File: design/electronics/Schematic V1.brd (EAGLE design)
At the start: 152.4 x 149.3 mm, 170 parts, among them J1 PJ-202AH, J2 PJ-025, J3 DD50P564GTXLF, J4 DD50P564GTXLF, J5 SAMTEC-TST-105-01-X-DJ, J6 SSW-106-02-TM-S-RA, SW1 TL6330AF200Q, U1 STM32F207VGT6TR, U10 SN65LBC175ADD16-M, U11 MAX7375AXR805+T21-0075D_MXM-M, U12 SN75ALS174ADWRDW20-M, U13 SN75468DRD0016A_M, U14 SN75468DRD0016A_M, U15 ACSL-6400-00TESOIC_6400-00TE-M, U16 ACSL-6400-00TESOIC_6400-00TE-M, U17 SN65LBC175ADD16-M, U18 SN65LBC175ADD16-M, U19 SN65LBC175ADD16-M, U2 LM2678S-5.0/NOPBTS7B-M, U21 RS0104YQTSSOP-14_JRT-M, U22 RS0104YQTSSOP-14_JRT-M, U24 RS0104YQTSSOP-14_JRT-M, U3 CDBC520-GCDBC-G-M, U4 TLV1117LV33DCYR, U5 LM43601PWPRPWP16_TEX-M, U6 RS0104YQTSSOP-14_JRT-M, U7 SN75ALS174ADWRDW20-M, U8 OPA4205APWRTSSOP14_PW_R-PDSO-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

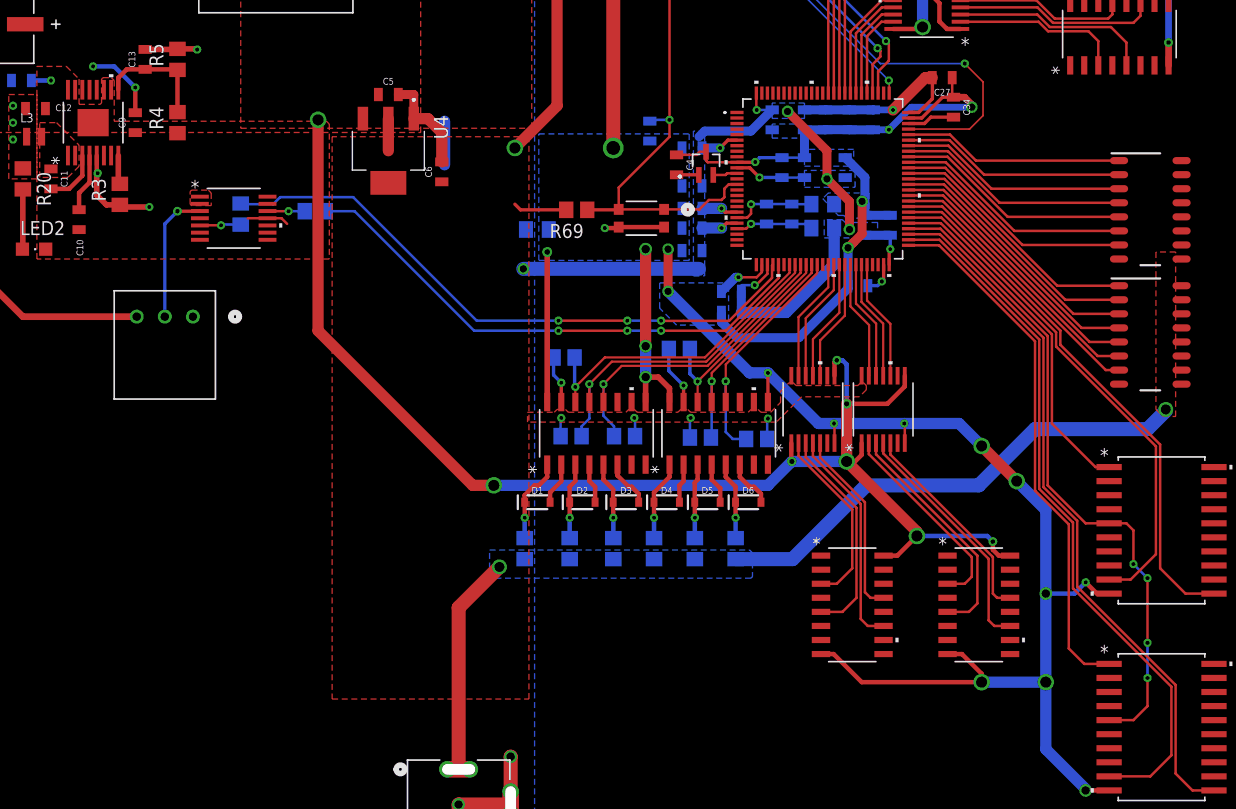
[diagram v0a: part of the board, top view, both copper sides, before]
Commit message: Updated Layout with most traces
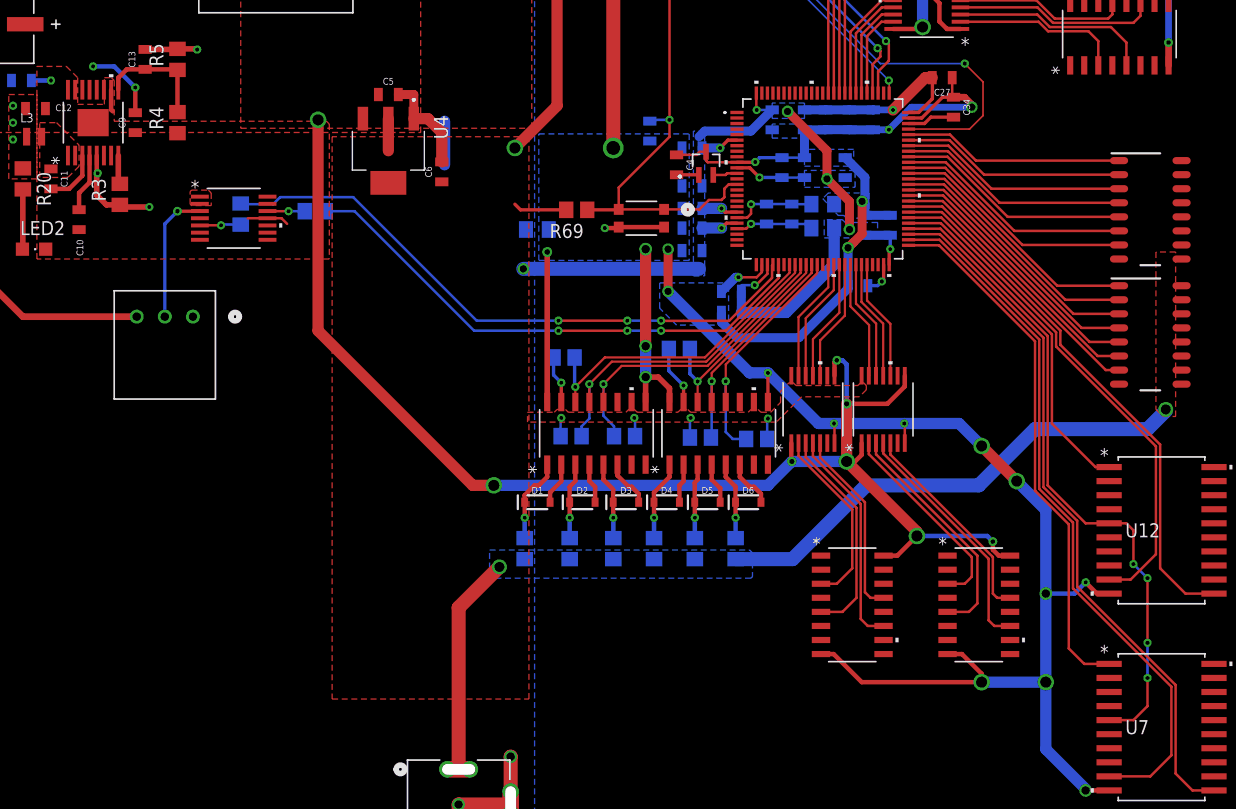
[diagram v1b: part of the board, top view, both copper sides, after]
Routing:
- net -15V: track 5.53 -> 7.55 mm
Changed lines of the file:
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@@
 <attribute name="MANUFACTURER_PART_NUMBER" value="SN75ALS174ADWR" x="306.07" y="-70.104" size="1.778" layer="27" display="off"/>
 <attribute name="MFR_NAME" value="Texas Instruments" x="306.07" y="-70.104" size="1.778" layer="27" display="off"/>
+<attribute name="NAME" x="112.2934" y="34.671" size="1.27" layer="27" ratio="6" rot="SR0"/>
 <attribute name="NAME" x="112.2934" y="34.671" size="1.27" layer="25" ratio="6" rot="SR0"/>
-<attribute name="NAME" x="112.2934" y="34.671" size="1.27" layer="27" ratio="6" rot="SR0"/>
 <attribute name="VALUE" x="113.8428" y="34.671" size="1.27" layer="27" ratio="6" rot="SR0"/>
 </element>
@@
 <attribute name="MANUFACTURER_PART_NUMBER" value="SN75ALS174ADWR" x="266.7" y="-87.884" size="1.778" layer="27" display="off"/>
 <attribute name="MFR_NAME" value="Texas Instruments" x="266.7" y="-87.884" size="1.778" layer="27" display="off"/>
+<attribute name="NAME" x="112.2934" y="16.891" size="1.27" layer="27" ratio="6" rot="SR0"/>
 <attribute name="NAME" x="112.2934" y="16.891" size="1.27" layer="25" ratio="6" rot="SR0"/>
-<attribute name="NAME" x="112.2934" y="16.891" size="1.27" layer="27" ratio="6" rot="SR0"/>
 <attribute name="VALUE" x="113.8428" y="16.891" size="1.27" layer="27" ratio="6" rot="SR0"/>
 </element>
@@
 <contactref element="C1" pad="2"/>
 <contactref element="C2" pad="1"/>
-<polygon width="0.1524" layer="1" isolate="0.508" thermals="no" rank="4">
+<polygon width="0.1524" layer="1" isolate="0.4064" thermals="no" rank="4">
 <vertex x="0" y="120.396"/>
 <vertex x="0" y="71.374"/>
@@
 <wire x1="11.176" y1="104.8258" x2="-15.56" y2="284.48" width="0" layer="19" extent="1-1"/>
 <wire x1="18.075" y1="75.1078" x2="18.725003125" y2="75.1078" width="0" layer="19" extent="1-1"/>
-<wire x1="19.375" y1="75.1078" x2="18.725003125" y2="75.1078" width="0" layer="19" extent="1-1"/>
 <wire x1="28.69565" y1="63.5" x2="22.86" y2="73.036" width="0" layer="19" extent="1-1"/>
 </signal>
@@
 <vertex x="13.97" y="77.216"/>
 <vertex x="16.637" y="77.216"/>
-<vertex x="17.78" y="76.073"/>
-<vertex x="17.78" y="73.787"/>
-<vertex x="19.685" y="73.787"/>
-<vertex x="19.812" y="73.914"/>
-<vertex x="19.812" y="76.073"/>
-<vertex x="19.939" y="76.2"/>
+<vertex x="17.653" y="76.2"/>
+<vertex x="17.653" y="73.787"/>
+<vertex x="20.066" y="73.787"/>
+<vertex x="20.066" y="76.2"/>
 <vertex x="20.701" y="76.2"/>
 <vertex x="20.955" y="75.946"/>
@@
 <wire x1="34.80435" y1="63.5" x2="36.068" y2="63.5" width="0.2286" layer="1"/>
 <wire x1="36.068" y1="63.5" x2="36.576" y2="62.992" width="0.2286" layer="1"/>
+<wire x1="20.675" y1="75.1078" x2="20.675" y2="73.305" width="0.4064" layer="1"/>
+<wire x1="20.675" y1="73.305" x2="20.828" y2="73.152" width="0.4064" layer="1"/>
 <wire x1="13.473" y1="75.946" x2="-124.46" y2="289.56" width="0" layer="19" extent="1-16"/>
-<wire x1="20.675" y1="75.1078" x2="17.425003125" y2="75.1078" width="0" layer="19" extent="1-1"/>
 </signal>
 <signal name="+24V">

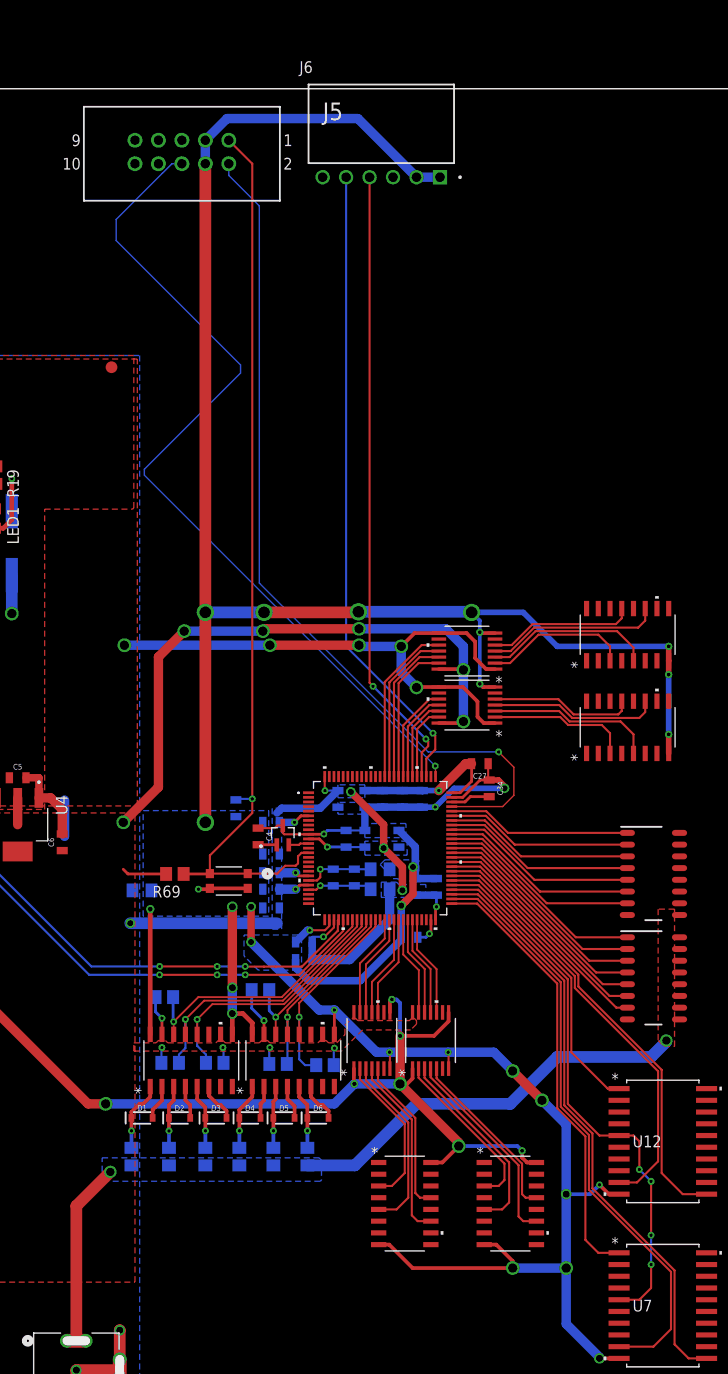
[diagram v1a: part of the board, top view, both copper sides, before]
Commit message: Moved UART signals to different pins for routing.
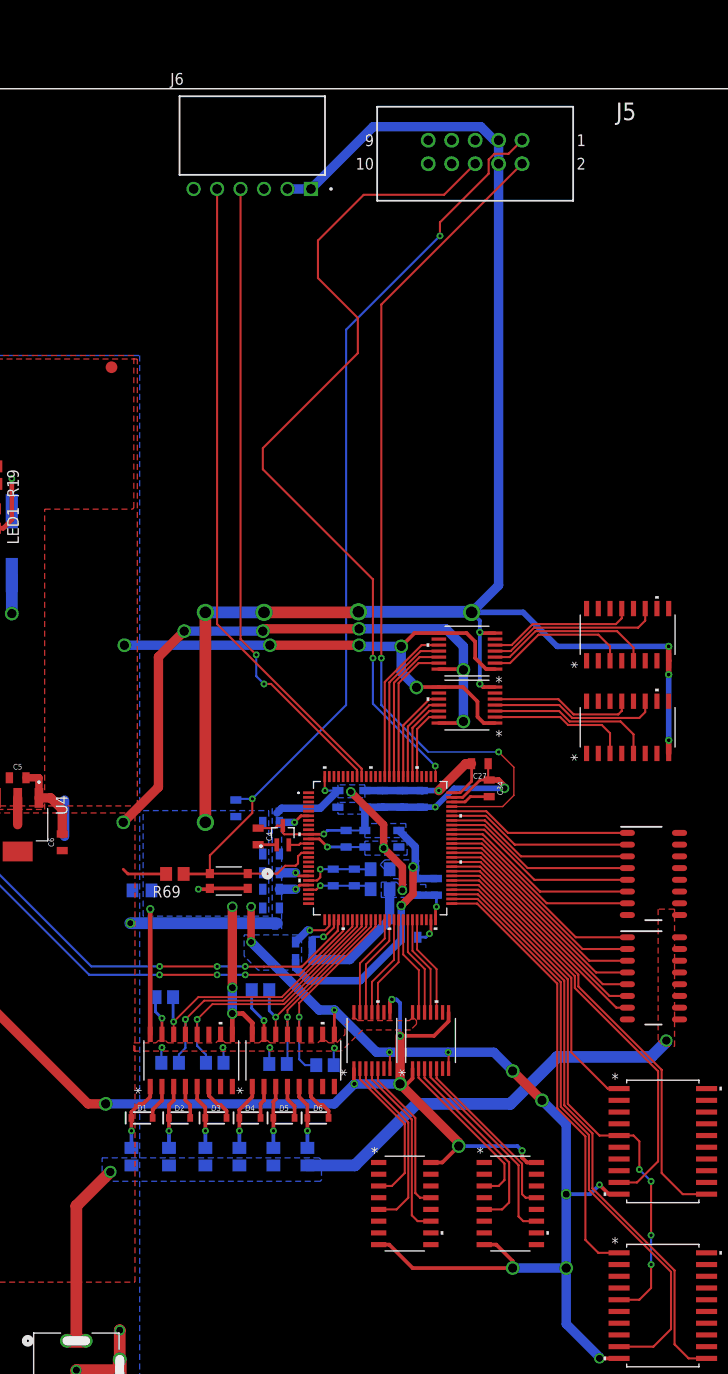
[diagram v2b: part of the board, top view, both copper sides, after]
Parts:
- moved J5 31.8 mm to (95.2, 142.2)
- moved J6 14.0 mm to (77.5, 138.4)
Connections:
- net UART_RX: now also U1.93; no longer U1.79
- net UART_TX: now also U1.92; no longer U1.78
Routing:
- net NRST: track 99.1 -> 111.0 mm, vias 1 -> 2
- net S_GND: track 404.7 -> 403.0 mm
- net UART_RX: track 67.8 -> 69.3 mm
- net UART_TX: track 69.3 -> 70.1 mm, vias 1 -> 0
- net SWCLK: track 92.9 -> 92.3 mm, vias 1 -> 2
- net SWDIO: track 92.9 -> 92.3 mm, vias 1 -> 2

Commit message: Updated schematic, added amazon order purchase
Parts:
- moved R34 344.2 mm to (94.7, 29.7), flipped to the bottom, turned to 45 degrees
- moved R33 340.6 mm to (103.9, 37.5), turned to 45 degrees
- moved R32 330.7 mm to (90.0, 32.0), flipped to the bottom, turned to 45 degrees
- moved R31 321.8 mm to (89.7, 38.0), flipped to the bottom, turned to 45 degrees
- moved C46 278.0 mm to (120.7, 47.0)
- moved C47 273.7 mm to (100.4, 43.3)
- moved J5 104.2 mm to (198.1, 125.7)
- moved J6 104.2 mm to (180.3, 121.9)
- moved U12 101.0 mm to (213.4, 9.91)
- moved U17 101.0 mm to (209.6, 64.8)
- moved U14 101.0 mm to (212.3, 38.9)
- moved R63 94.8 mm to (145.7, -8.00)
- moved U16 93.8 mm to (148.0, -15.6)
- moved D6 93.8 mm to (150.6, -21.8)
- moved R30 93.8 mm to (149.5, -26.0)
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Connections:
- net ABS_ENC_OUT_GPIO_1: now also U1.44; no longer U1.83
- net ABS_ENC_OUT_GPIO_2: no longer U1.87
- net ALARM_RST_AN_1: now also U13.14; no longer U13.12
- net ALARM_RST_GPIO_1: now also U1.38, U13.3; no longer U1.60, U13.5
- net ALARM_RST_GPIO_2: no longer U1.67
- net ALO_GPIO_A_1: now also U1.31; no longer U1.32
- net ALO_GPIO_A_2: no longer U1.35
- net ALO_GPIO_B_1: now also U1.32; no longer U1.33
- net ALO_GPIO_B_2: no longer U1.36
- net ALO_GPIO_C_1: now also U1.33; no longer U1.34
- net ALO_GPIO_C_2: no longer U1.37
- net CLR_GPIO_2: no longer U1.57
- net DIR_GPIO_2: no longer U1.56
- net ENC_PUL_OUT_A_GPIO_1: now also U1.41; no longer U1.80
- net ENC_PUL_OUT_A_GPIO_2: no longer U1.84
- net ENC_PUL_OUT_B_GPIO_1: now also U1.42; no longer U1.81
- net ENC_PUL_OUT_B_GPIO_2: no longer U1.85
- net ENC_PUL_OUT_C_GPIO_1: now also U1.43; no longer U1.82
- net ENC_PUL_OUT_C_GPIO_2: no longer U1.86
- net FRWD_DRIVE_EN_AN_1: now also U13.12; no longer U13.14
- net FRWD_DRIVE_EN_GPIO_1: now also U1.36, U13.5; no longer U1.62, U13.3
- net FRWD_DRIVE_EN_GPIO_2: no longer U1.69
- net FRWD_EX_TORQUE_LIM_EN_AN_1: now also U13.15; no longer U13.11
- net FRWD_EX_TORQUE_LIM_EN_GPIO_1: now also U1.39, U13.2; no longer U1.59, U13.6
- net FRWD_EX_TORQUE_LIM_EN_GPIO_2: no longer U1.66
- net GEN_PURPOSE_OUT_GPIO_A_1: now also U1.45; no longer U1.39
- net GEN_PURPOSE_OUT_GPIO_A_2: no longer U1.43
- net GEN_PURPOSE_OUT_GPIO_B_1: now also U1.46; no longer U1.40
- net GEN_PURPOSE_OUT_GPIO_B_2: no longer U1.44
- net GEN_PURPOSE_OUT_GPIO_C_1: now also U1.47; no longer U1.41
- net GEN_PURPOSE_OUT_GPIO_C_2: no longer U1.45
- net PROP_CONTROL_EN_AN_1: now also U13.11; no longer U13.15
- net PROP_CONTROL_EN_GPIO_1: now also U1.35, U13.6; no longer U1.63, U13.2
- net PROP_CONTROL_EN_GPIO_2: no longer U1.70
- net PULSE_GPIO_2: no longer U1.55
- net REVERSE_DRIVE_EN_GPIO_1: now also U1.37; no longer U1.61
- net REVERSE_DRIVE_EN_GPIO_2: no longer U1.68
- net REVERSE_EX_TORQUE_LIM_EN_AN_1: now also U13.16; no longer U13.10
- net REVERSE_EX_TORQUE_LIM_EN_GPIO_1: now also U1.40, U13.1; no longer U1.58, U13.7
- net REVERSE_EX_TORQUE_LIM_EN_GPIO_2: no longer U1.65
- net SERVO_ALARM_OUT_GPIO_1: now also U1.48; no longer U1.42
- net SERVO_ALARM_OUT_GPIO_2: no longer U1.46
- net SERVO_EN_AN_1: now also U13.10; no longer U13.16
- net SERVO_EN_GPIO_1: now also U1.34, U13.7; no longer U1.64, U13.1
- net SERVO_EN_GPIO_2: no longer U1.71
- net UART_RX: no longer U1.93
- net UART_TX: no longer U1.92
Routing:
- net S_GND: track 403.0 -> 161.6 mm, vias 33 -> 20
- net ENC_PUL_OUT_A_HI_1: track 0.00 -> 102.7 mm, vias 0 -> 4
- net TORQUE-SPEED_ANALOG_1: track 0.00 -> 102.4 mm, vias 0 -> 1
- net SWDIO: track 92.3 -> 0.00 mm, vias 2 -> 0
- net SWCLK: track 92.3 -> 0.00 mm, vias 2 -> 0
- net NRST: track 111.0 -> 26.7 mm, vias 2 -> 1
- net P_GND: track 77.0 -> 161.1 mm, vias 17 -> 19
- net +3.3V: track 192.9 -> 116.7 mm, vias 24 -> 14
- net UART_TX: track 70.1 -> 0.00 mm
- net UART_RX: track 69.3 -> 0.00 mm, vias 2 -> 0
- net +24V: track 64.4 -> 133.1 mm, vias 2 -> 3
- net CLR_LO_1: track 0.00 -> 62.1 mm, vias 0 -> 2
- net ALO_AN_C_1: track 4.34 -> 58.0 mm
- net CLR_HI_1: track 0.00 -> 51.8 mm, vias 0 -> 1
- net ALO_AN_B_1: track 3.61 -> 52.8 mm, vias 0 -> 1
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- removed copper zone on layer 1, net +24V
- removed copper zone on layer 16, net +24V

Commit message: Updated Layout more
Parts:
- added R23, R25: 66k, rcl:R0805
- added R24, R6: 33k, rcl:R0805
- moved R49 481.2 mm to (157.5, 5.08)
- moved R43 473.1 mm to (189.2, 10.2)
- moved R44 473.1 mm to (182.9, 10.2)
- moved R45 473.1 mm to (176.5, 10.2)
- moved R46 473.1 mm to (170.2, 10.2)
- moved R47 473.1 mm to (163.8, 10.2)
- moved R48 473.1 mm to (157.5, 10.2)
- moved R42 470.9 mm to (187.5, 2.51), turned to 90 degrees
- moved R41 386.2 mm to (109.2, 31.5), flipped to the bottom, turned to 90 degrees
- moved R40 377.7 mm to (110.0, 38.1), turned to 90 degrees
- moved R39 370.9 mm to (107.4, 38.1), turned to 90 degrees
- moved C51 343.9 mm to (182.9, 22.9)
- moved C52 343.9 mm to (179.1, 22.9)
- moved C53 343.9 mm to (175.3, 22.9)
- moved C50 292.4 mm to (107.0, 31.5), flipped to the bottom, turned to 90 degrees
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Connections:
- removed net V_ON: R1.2, R2.1, U10.12, U10.4, U12.15, U17.12, U17.4, U18.12, U18.4, U19.12, U19.4, U2.7, U7.15
- new net V_ON_14V: R1.2, R2.1, U2.7
- new net V_ON_5V: U10.12, U12.15, U17.12, U17.4, U19.12, U19.4
- new net V_ON_5V_1: R23.2, R6.1, U10.4, U18.12, U18.4
- new net V_ON_5V_2: R24.1, R25.2, U7.15
- net +5V: now also R24.2, R6.2
- net S_GND: now also R23.1, R25.1
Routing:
- net S_GND: track 161.6 -> 238.0 mm, vias 20 -> 23
- net +3.3V: track 116.7 -> 137.0 mm, vias 14 -> 16
- net ALO_AN_A_2: track 0.00 -> 17.8 mm
- net V_ON_5V_1: track 0.00 -> 8.95 mm, vias 0 -> 2
- net V_ON: track 7.86 -> 0.00 mm
- net GEN_PURPOSE_OUT_LO_A_1: track 29.0 -> 36.5 mm, vias 1 -> 3
- net +5V: track 151.1 -> 158.2 mm, vias 7 -> 9
- net V_ON_14V: track 0.00 -> 6.39 mm
- net V_ON_5V_2: track 0.00 -> 5.98 mm, vias 0 -> 1
- net PULSE_HI_1: track 46.3 -> 51.9 mm
- net PULSE_LO_1: track 46.6 -> 51.9 mm
- net GEN_PURPOSE_OUT_HI_A_1: track 30.4 -> 33.4 mm
- net ABS_ENC_OUT_LO_1: track 39.9 -> 41.7 mm, vias 5 -> 3
- net DIR_HI_1: track 44.6 -> 43.6 mm
- net ABS_ENC_OUT_HI_1: track 38.0 -> 38.7 mm

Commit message: Layout almost done
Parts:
- added R26, R71, R73: 33k, rcl:R0805
- added R70, R72, R74: 66k, rcl:R0805
- moved R50 441.6 mm to (115.4, 23.0)
- moved R51 371.7 mm to (76.9, 104.1)
- moved H2 312.1 mm to (146.2, 6.02), flipped to the bottom
- moved R38 306.2 mm to (91.1, 116.4), flipped to the bottom, turned to 225 degrees
- moved H1 300.7 mm to (6.35, 6.35)
- moved C54 299.8 mm to (111.4, 34.2), flipped to the bottom, turned to 90 degrees
- moved R36 299.2 mm to (92.6, 111.8), flipped to the bottom, turned to 225 degrees
- moved R35 296.5 mm to (90.4, 104.4), flipped to the bottom, turned to 90 degrees
- moved R37 289.1 mm to (78.5, 118.5), flipped to the bottom, turned to 315 degrees
- moved C60 265.5 mm to (115.8, 98.6), turned to 180 degrees
- moved C61 260.6 mm to (105.4, 99.1), turned to 270 degrees
- moved C48 241.0 mm to (120.0, 95.5), turned to 270 degrees
- moved LED3 238.3 mm to (-100.3, 41.9)
- moved LED4 238.3 mm to (-106.7, 41.9)
- moved R21 238.3 mm to (-16.5, 59.7)
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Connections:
- new net V_ON_5V_3: R26.1, R70.2, U10.12, U10.4
- new net V_ON_5V_4: R71.1, R72.2, U17.12, U17.4
- new net V_ON_5V_5: R73.1, R74.2, U19.12, U19.4
- net +5V: now also R26.2, R71.2, R73.2
- net ABS_ENC_OUT_GPIO_2: now also U1.90
- net ALARM_RST_GPIO_2: now also U1.84
- net ALO_GPIO_A_2: now also U1.77
- net ALO_GPIO_B_2: now also U1.78
- net ALO_GPIO_C_2: now also U1.79
- net CLR_GPIO_1: now also U1.54; no longer U1.53
- net CLR_GPIO_2: now also U1.69
- net DIR_GPIO_1: now also U1.53; no longer U1.52
- net DIR_GPIO_2: now also U1.71
- net ENC_PUL_OUT_A_GPIO_2: now also U1.87
- net ENC_PUL_OUT_B_GPIO_2: now also U1.88
- net ENC_PUL_OUT_C_GPIO_2: now also U1.89
- net FRWD_DRIVE_EN_GPIO_2: now also U1.82
- net FRWD_EX_TORQUE_LIM_EN_GPIO_2: now also U1.85
- net GEN_PURPOSE_OUT_GPIO_A_2: now also U1.91
- net GEN_PURPOSE_OUT_GPIO_B_2: now also U1.92
- net GEN_PURPOSE_OUT_GPIO_C_2: now also U1.93
- net POS_EN_GPIO: now also U1.55; no longer U1.54
- net PROP_CONTROL_EN_GPIO_2: now also U1.81
- net PULSE_GPIO_1: now also U1.52; no longer U1.51
- net PULSE_GPIO_2: now also U1.70
- net REVERSE_DRIVE_EN_GPIO_2: now also U1.83
- net REVERSE_EX_TORQUE_LIM_EN_GPIO_2: now also U1.86
- net SERVO_ALARM_OUT_GPIO_2: now also U1.95
- net SERVO_EN_GPIO_2: now also U1.80
- net S_GND: now also R70.1, R72.1, R74.1
- net UART_RX: now also U1.64
- net UART_TX: now also U1.63
- net V_ON_5V: no longer U10.12, U17.12, U17.4, U19.12, U19.4
- net V_ON_5V_1: no longer U10.4
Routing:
- net +14V: track 28.4 -> 384.6 mm, vias 6 -> 20
- net +24V: track 133.1 -> 447.8 mm, vias 3 -> 4
- net S_GND: track 238.0 -> 495.2 mm, vias 23 -> 34
- net +5V: track 158.2 -> 320.8 mm, vias 9 -> 21
- net NRST: track 26.7 -> 125.9 mm
- net CLR_HI_2: track 0.00 -> 95.0 mm
- net CLR_LO_2: track 0.00 -> 92.5 mm, vias 0 -> 1
- net +3.3V: track 137.0 -> 227.5 mm, vias 16 -> 19
- net DIR_LO_2: track 0.00 -> 72.5 mm, vias 0 -> 1
- net DIR_HI_2: track 0.00 -> 71.2 mm, vias 0 -> 1
- net P_GND: track 161.1 -> 231.1 mm
- net PULSE_GPIO_2: track 0.00 -> 62.6 mm
- net PULSE_LO_2: track 0.00 -> 60.0 mm, vias 0 -> 1
- net POS_EN_GPIO: track 47.9 -> 106.1 mm, vias 2 -> 6
- net PULSE_HI_2: track 0.00 -> 56.2 mm, vias 0 -> 1
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- added copper zone on layer 1, net GEN_PURPOSE_OUT_LO_C_2
- added copper zone on layer 1, net S_GND
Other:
- board size 152.4 x 149.3 mm -> 152.4 x 139.7 mm
